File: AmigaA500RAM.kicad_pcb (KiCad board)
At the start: 4 copper layers, 73 x 72.4 mm, 41 parts, among them J1 SSQ-128-02-G-D-RA, U1 74LVC16T245, U2 TLV1117LV33, U3 SN74LVC821A, U4 SN74LVC821A, U5 SN74LVC244A, U6 SN74LVC00A, U7 AS6C6416-55TIN

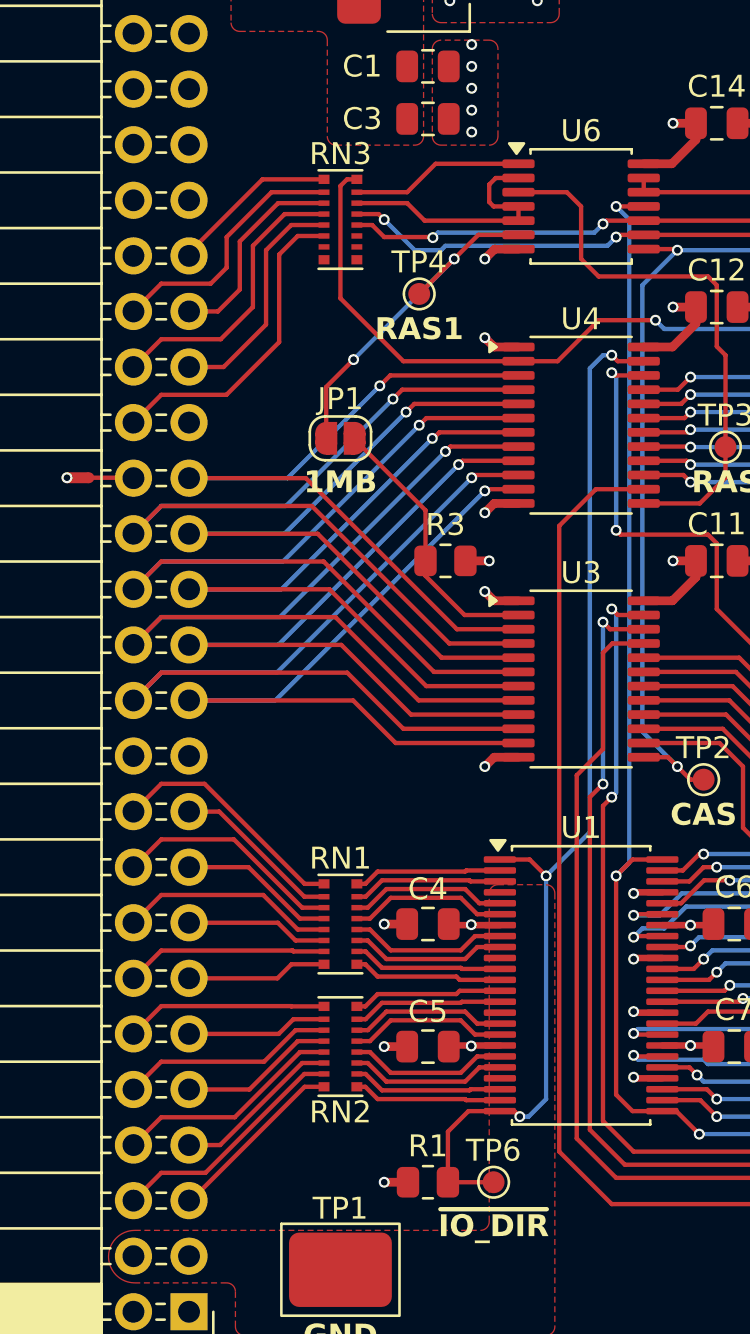
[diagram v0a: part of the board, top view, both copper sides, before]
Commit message: Update resistor arrays to 4x0603
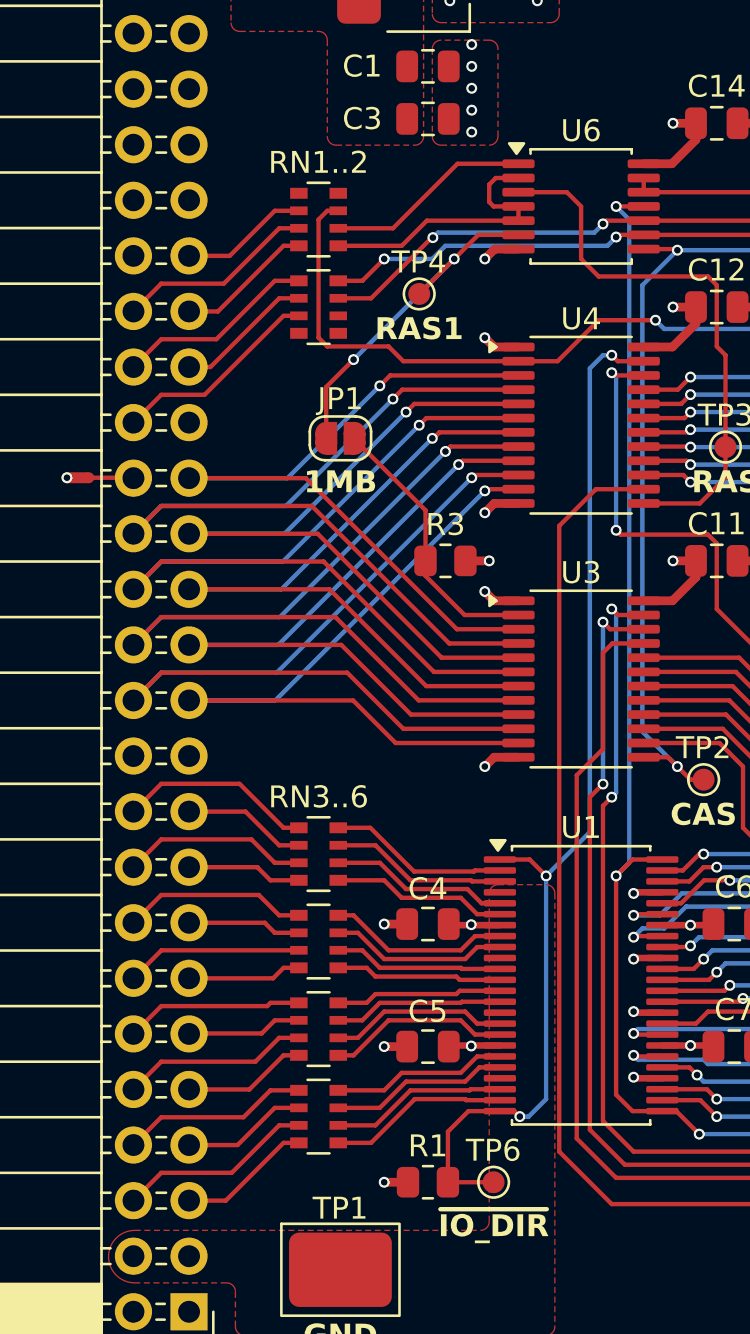
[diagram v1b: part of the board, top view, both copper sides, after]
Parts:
- added RN4: YC164-FR-0768, Resistor_SMD:R_Array_Convex_4x0603, F.Cu at (138.0, 105.0)
- added RN5: YC164-FR-0768, Resistor_SMD:R_Array_Convex_4x0603, F.Cu at (138.0, 109.0)
- added RN6: YC164-FR-0768, Resistor_SMD:R_Array_Convex_4x0603, F.Cu at (138.0, 113.0)
- RN1..2: renamed from RN1; value EXB-2HV680JV -> YC164-FR-0768; footprint AmigaA500RAM:R_Array08_EXB2H -> Resistor_SMD:R_Array_Convex_4x0603
- RN2: value EXB-2HV680JV -> YC164-FR-0768; footprint AmigaA500RAM:R_Array08_EXB2H -> Resistor_SMD:R_Array_Convex_4x0603
- RN3..6: renamed from RN3; value EXB-2HV680JV -> YC164-FR-0768; footprint AmigaA500RAM:R_Array08_EXB2H -> Resistor_SMD:R_Array_Convex_4x0603
- moved RN2 33.8 mm to (138.0, 76.0)
- moved RN1..2 32.2 mm to (138.0, 72.0)
- moved RN3..6 29.0 mm to (138.0, 101.0)
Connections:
- RN1..2 pad 1: XDRD15 -> unconnected-(RN1-R1.1-Pad1)
- RN1..2 pad 2: XDRD14 -> ~{XWE}
- RN1..2 pad 3: XDRD13 -> ~{XRAS0}
- RN1..2 pad 4: XDRD12 -> ~{XRAS1}
- RN1..2 pad 5: XDRD11 -> Net-(RN1-R4.2)
- RN1..2 pad 6: XDRD10 -> Net-(RN1-R3.2)
- RN1..2 pad 7: XDRD9 -> ~{WE}
- RN1..2 pad 8: XDRD8 -> unconnected-(RN1-R1.2-Pad8)
- RN2 pad 1: XDRD7 -> ~{XCASU}
- RN2 pad 2: XDRD6 -> ~{XCASL}
- RN2 pad 3: XDRD5 -> ~{XOE}
- RN2 pad 4: XDRD4 -> unconnected-(RN2-R4.1-Pad4)
- RN2 pad 5: XDRD3 -> unconnected-(RN2-R4.2-Pad5)
- RN2 pad 6: XDRD2 -> unconnected-(RN2-R3.2-Pad6)
- RN2 pad 7: XDRD1 -> ~{CASL}
- RN2 pad 8: XDRD0 -> ~{CASU}
- RN3..6 pad 1: ~{XWE} -> XDRD15
- RN3..6 pad 2: ~{XRAS0} -> XDRD14
- RN3..6 pad 3: ~{XRAS1} -> XDRD13
- RN3..6 pad 4: ~{XCASU} -> XDRD12
- RN3..6 pad 5: ~{XCASL} -> Net-(RN3-R4.2)
- RN3..6 pad 6: ~{XOE} -> Net-(RN3-R3.2)
- RN3..6 pad 7: unconnected-(RN3-R7.1-Pad7) -> Net-(RN3-R2.2)
- RN3..6 pad 8: unconnected-(RN3-R8.1-Pad8) -> Net-(RN3-R1.2)
- U1 pad 11: Net-(RN1-R7.2) -> Net-(RN4-R3.2)
- U1 pad 12: Net-(RN1-R8.2) -> Net-(RN4-R4.2)
- U1 pad 13: Net-(RN2-R1.2) -> Net-(RN5-R1.2)
- U1 pad 14: Net-(RN2-R2.2) -> Net-(RN5-R2.2)
- U1 pad 16: Net-(RN2-R3.2) -> Net-(RN5-R3.2)
- U1 pad 17: Net-(RN2-R4.2) -> Net-(RN5-R4.2)
- U1 pad 19: Net-(RN2-R5.2) -> Net-(RN6-R1.2)
- U1 pad 2: Net-(RN1-R1.2) -> Net-(RN3-R1.2)
- U1 pad 20: Net-(RN2-R6.2) -> Net-(RN6-R2.2)
- U1 pad 22: Net-(RN2-R7.2) -> Net-(RN6-R3.2)
- U1 pad 23: Net-(RN2-R8.2) -> Net-(RN6-R4.2)
- U1 pad 3: Net-(RN1-R2.2) -> Net-(RN3-R2.2)
- U1 pad 5: Net-(RN1-R3.2) -> Net-(RN3-R3.2)
- U1 pad 6: Net-(RN1-R4.2) -> Net-(RN3-R4.2)
- U1 pad 8: Net-(RN1-R5.2) -> Net-(RN4-R1.2)
- U1 pad 9: Net-(RN1-R6.2) -> Net-(RN4-R2.2)
- U6 pad 1: Net-(RN3-R2.2) -> Net-(RN1-R3.2)
- U6 pad 2: Net-(RN3-R3.2) -> Net-(RN1-R4.2)
- U6 pad 4: Net-(RN3-R3.2) -> Net-(RN1-R4.2)
- U6 pad 5: Net-(RN3-R3.2) -> Net-(RN1-R4.2)
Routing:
- net Net-(RN5-R4.2): track 0.00 -> 8.32 mm
- net Net-(RN4-R1.2): track 0.00 -> 8.32 mm
- net Net-(RN6-R4.2): track 0.00 -> 8.24 mm
- net Net-(RN3-R1.2): track 0.00 -> 8.23 mm
- net Net-(RN6-R2.2): track 0.00 -> 8.15 mm
- net Net-(RN5-R3.2): track 0.00 -> 8.11 mm
- net Net-(RN4-R2.2): track 0.00 -> 8.11 mm
- net Net-(RN6-R3.2): track 0.00 -> 8.07 mm
- net Net-(RN6-R1.2): track 0.00 -> 8.03 mm
- net Net-(RN3-R4.2): track 0.00 -> 8.03 mm
- net Net-(RN5-R2.2): track 0.00 -> 7.74 mm
- net Net-(RN4-R3.2): track 0.00 -> 7.74 mm
- net Net-(RN5-R1.2): track 0.00 -> 7.62 mm
- net Net-(RN4-R4.2): track 0.00 -> 7.62 mm
- net Net-(RN2-R5.2): track 7.24 -> 0.00 mm
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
